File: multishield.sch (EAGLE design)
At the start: 18 parts, among them CN1 3P-2.54-90D, J2 2x16p-2.54, J4 2x6p-2.54, K2 TS-1101F, M1 ARDUINO_R3_ICSP, SW1 SK-12D01, U1 AD595AQ-DIP14, U2 ATMEGA328P_PDIP, Y1 16MHZ

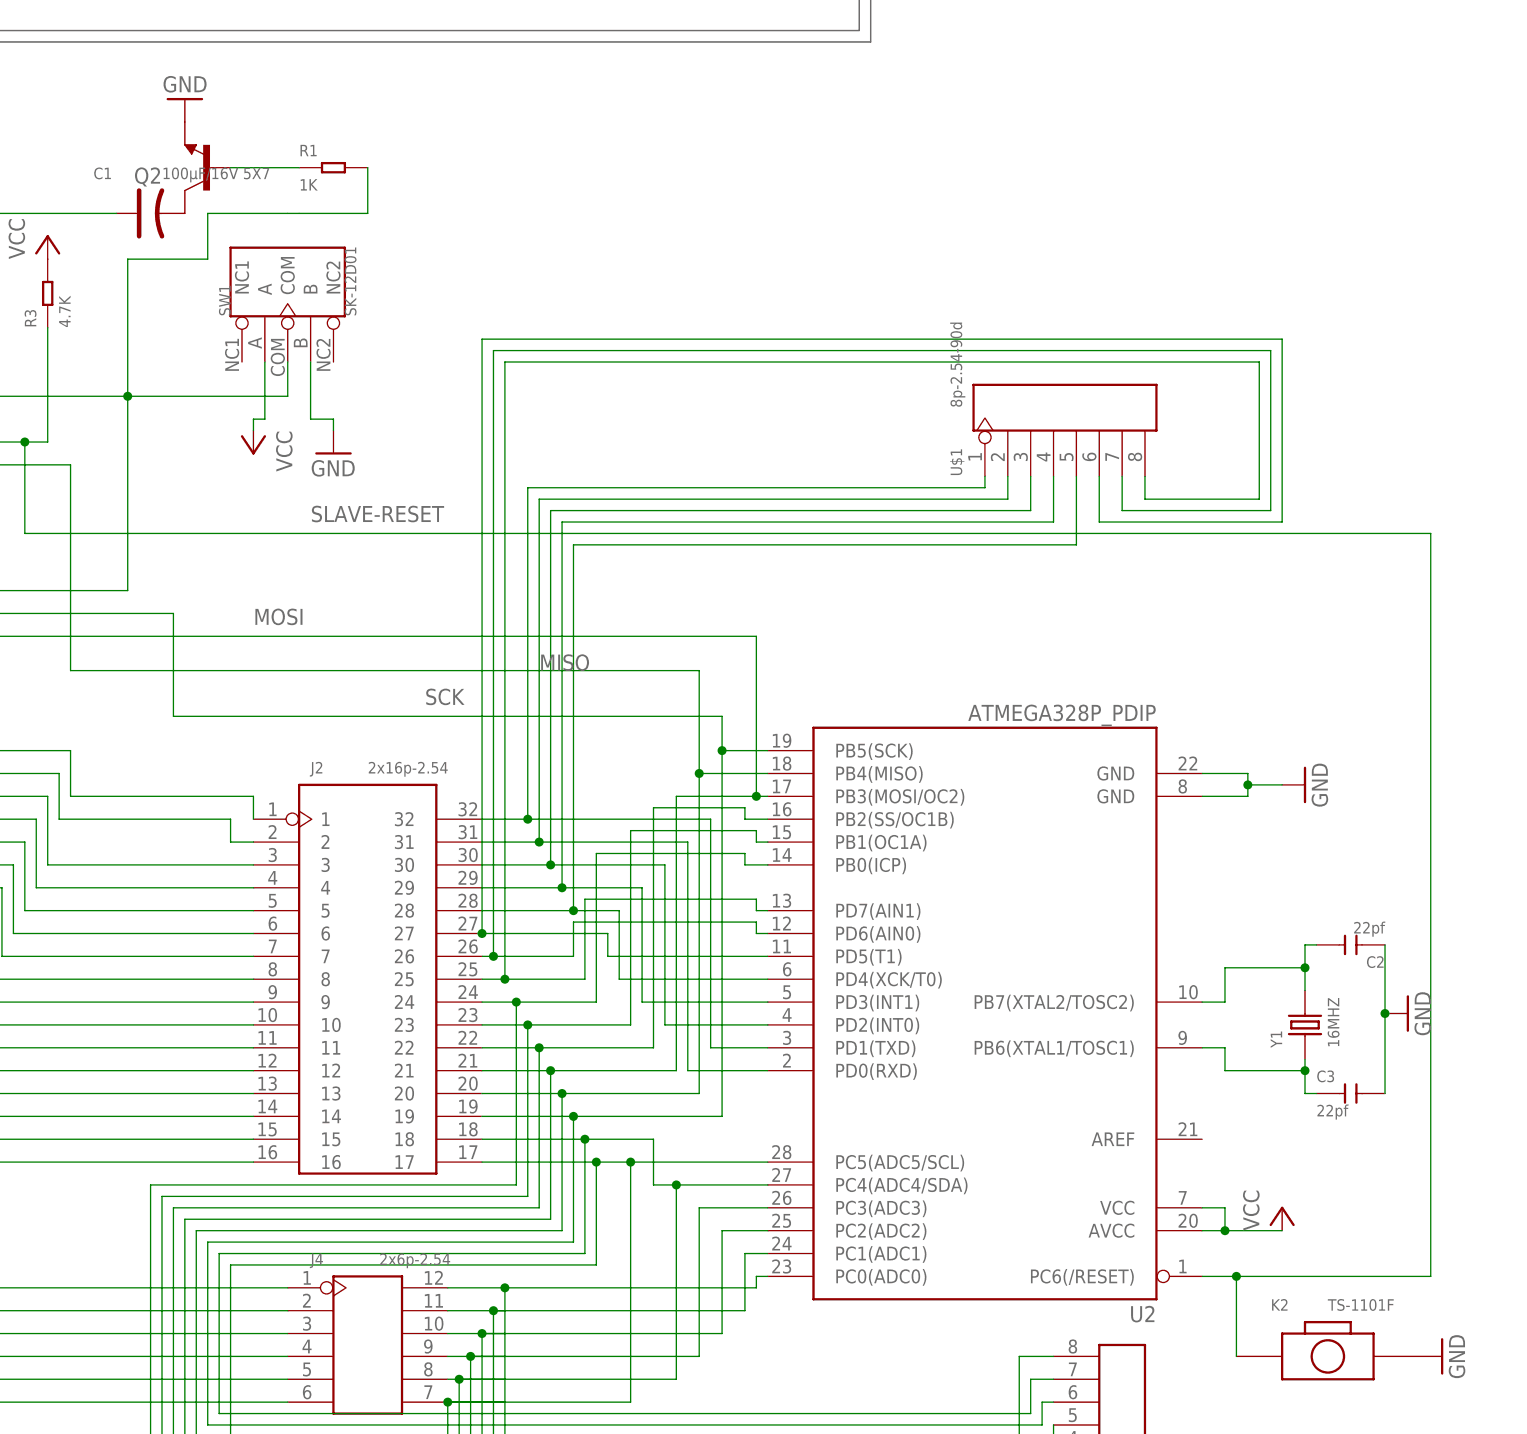
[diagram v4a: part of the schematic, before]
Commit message: adding 100nF capacitors and minor other changes
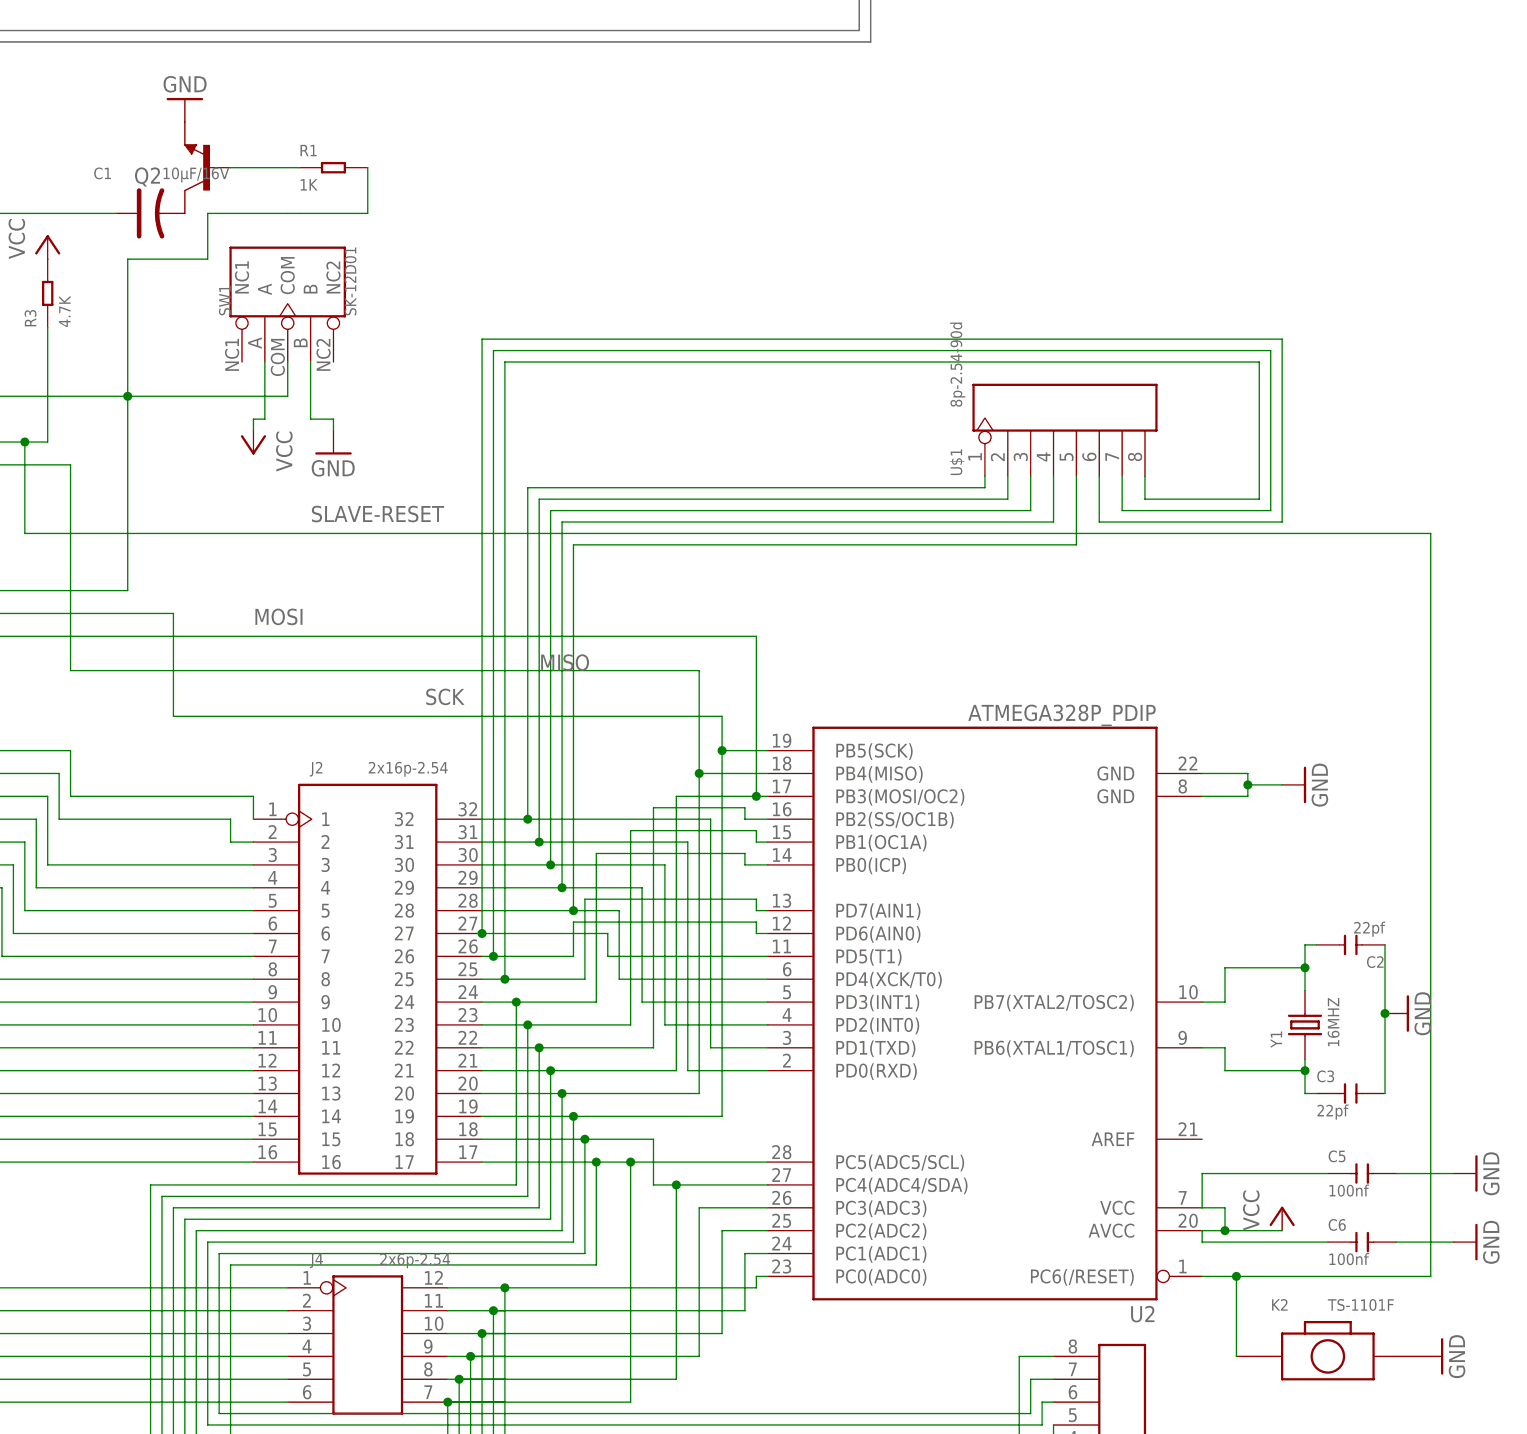
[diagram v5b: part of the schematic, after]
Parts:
- added C5, C6: 100nf, Seeed-OPL-Capacitor:DIP-CERAMIC-DISC-100NF-50V-Y5V(D5.0MM)
- C1: value 100µF/16V 5X7 -> 10µF/16V
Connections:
- net GND: now also C5.2, C6.2
- net VCC: now also C5.1, C6.1
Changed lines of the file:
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@@
 <setting verticaltext="up"/>
 </settings>
-<grid distance="0.05" unitdist="inch" unit="inch" style="lines" multiple="1" display="no" altdistance="0.01" altunitdist="inch" altunit="inch"/>
+<grid distance="0.1" unitdist="inch" unit="inch" style="lines" multiple="1" display="no" altdistance="0.01" altunitdist="inch" altunit="inch"/>
 <layers>
 <layer number="1" name="Top" color="4" fill="1" visible="no" active="no"/>
@@
 <part name="GND11" library="supply1" deviceset="GND" device=""/>
 <part name="K2" library="Seeed-OPL-Button" deviceset="DIP-BUTTON-FRONT-WHITE(2P-3.4X6MM)" device="" value="TS-1101F"/>
-<part name="C1" library="Seeed-OPL-Capacitor" deviceset="DIP-CAP-ALUMINUM-47UF-16V(D5-H9MM)" device="" value="100µF/16V  5X7"/>
+<part name="C1" library="Seeed-OPL-Capacitor" deviceset="DIP-CAP-ALUMINUM-47UF-16V(D5-H9MM)" device="" value="10µF/16V"/>
 <part name="GND5" library="supply1" deviceset="GND" device=""/>
 <part name="R1" library="Seeed-OPL-Resistor" deviceset="DIP-RES-1K-5%-1/4W(PR-D2.3XL6.5MM)" device="" value="1K"/>
@@
 <part name="Q2" library="SparkFun-DiscreteSemi" deviceset="TRANSISTOR_NPN" device="BC547"/>
 <part name="CN1" library="Seeed-OPL-Connector" deviceset="DIP-BLACK-FEMALE-HEADER(3P-2.54-90D)" device="" value="3P-2.54-90D"/>
+<part name="C5" library="Seeed-OPL-Capacitor" deviceset="DIP-CERAMIC-DISC-100NF-50V-Y5V(D5.0MM)" device="" value="100nf"/>
+<part name="C6" library="Seeed-OPL-Capacitor" deviceset="DIP-CERAMIC-DISC-100NF-50V-Y5V(D5.0MM)" device="" value="100nf"/>
+<part name="GND12" library="supply1" deviceset="GND" device=""/>
+<part name="GND13" library="supply1" deviceset="GND" device=""/>
 </parts>
 <sheets>
@@
 <instance part="Q2" gate="G$1" x="194.31" y="177.8" rot="R180"/>
 <instance part="CN1" gate="G$1" x="97.79" y="69.85"/>
+<instance part="C5" gate="G$1" x="322.58" y="66.04"/>
+<instance part="C6" gate="G$1" x="322.58" y="58.42"/>
+<instance part="GND12" gate="1" x="335.28" y="66.04" rot="R90"/>
+<instance part="GND13" gate="1" x="335.28" y="58.42" rot="R90"/>
 </instances>
 <busses>
@@
 <pinref part="U2" gate="G$1" pin="AVCC"/>
 <pinref part="P+2" gate="VCC" pin="VCC"/>
+<junction x="307.34" y="59.69"/>
 <wire x1="304.8" y1="59.69" x2="307.34" y2="59.69" width="0.1524" layer="91"/>
-<junction x="307.34" y="59.69"/>
 <wire x1="307.34" y1="59.69" x2="313.69" y2="59.69" width="0.1524" layer="91"/>
 <pinref part="U2" gate="G$1" pin="VCC"/>
 <wire x1="304.8" y1="62.23" x2="307.34" y2="62.23" width="0.1524" layer="91"/>
 <wire x1="307.34" y1="62.23" x2="307.34" y2="59.69" width="0.1524" layer="91"/>
+<pinref part="C5" gate="G$1" pin="1"/>
+<wire x1="318.77" y1="66.04" x2="304.8" y2="66.04" width="0.1524" layer="91"/>
+<wire x1="304.8" y1="66.04" x2="304.8" y2="62.23" width="0.1524" layer="91"/>
+<pinref part="C6" gate="G$1" pin="1"/>
+<wire x1="318.77" y1="58.42" x2="304.8" y2="58.42" width="0.1524" layer="91"/>
+<wire x1="304.8" y1="58.42" x2="304.8" y2="59.69" width="0.1524" layer="91"/>
 </segment>
 <segment>
@@
 <pinref part="CN1" gate="G$1" pin="P$3"/>
 </segment>
-</net>
+<segment>
+<pinref part="C5" gate="G$1" pin="2"/>
+<pinref part="GND12" gate="1" pin="GND"/>
+<wire x1="332.74" y1="66.04" x2="326.39" y2="66.04" width="0.1524" layer="91"/>
+</segment>
+<segment>
+<pinref part="C6" gate="G$1" pin="2"/>
+<pinref part="GND13" gate="1" pin="GND"/>
+<wire x1="332.74" y1="58.42" x2="326.39" y2="58.42" width="0.1524" layer="91"/>
+</segment>
+</net>

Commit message: rev 1
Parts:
- C1: value 10µF/16V -> 10µF
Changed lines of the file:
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@@
 <part name="GND11" library="supply1" deviceset="GND" device=""/>
 <part name="K2" library="Seeed-OPL-Button" deviceset="DIP-BUTTON-FRONT-WHITE(2P-3.4X6MM)" device="" value="TS-1101F"/>
-<part name="C1" library="Seeed-OPL-Capacitor" deviceset="DIP-CAP-ALUMINUM-47UF-16V(D5-H9MM)" device="" value="10µF/16V"/>
+<part name="C1" library="Seeed-OPL-Capacitor" deviceset="DIP-CAP-ALUMINUM-47UF-16V(D5-H9MM)" device="" value="10µF"/>
 <part name="GND5" library="supply1" deviceset="GND" device=""/>
 <part name="R1" library="Seeed-OPL-Resistor" deviceset="DIP-RES-1K-5%-1/4W(PR-D2.3XL6.5MM)" device="" value="1K"/>

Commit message: latest updates
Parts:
- added J1, J3, J5, J6: 7p-2.54-90d, Seeed-OPL-Connector:DIP-BLACK-MALE-HEADER(7P-2.54-90D)
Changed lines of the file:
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@@
 <setting verticaltext="up"/>
 </settings>
-<grid distance="0.1" unitdist="inch" unit="inch" style="lines" multiple="1" display="no" altdistance="0.01" altunitdist="inch" altunit="inch"/>
+<grid distance="0.05" unitdist="inch" unit="inch" style="lines" multiple="1" display="no" altdistance="0.01" altunitdist="inch" altunit="inch"/>
 <layers>
 <layer number="1" name="Top" color="4" fill="1" visible="no" active="no"/>
@@
 <part name="GND12" library="supply1" deviceset="GND" device=""/>
 <part name="GND13" library="supply1" deviceset="GND" device=""/>
+<part name="J1" library="Seeed-OPL-Connector" deviceset="DIP-BLACK-MALE-HEADER(7P-2.54-90D)" device="" value="7p-2.54-90d"/>
+<part name="J3" library="Seeed-OPL-Connector" deviceset="DIP-BLACK-MALE-HEADER(7P-2.54-90D)" device="" value="7p-2.54-90d"/>
+<part name="J5" library="Seeed-OPL-Connector" deviceset="DIP-BLACK-MALE-HEADER(7P-2.54-90D)" device="" value="7p-2.54-90d"/>
+<part name="J6" library="Seeed-OPL-Connector" deviceset="DIP-BLACK-MALE-HEADER(7P-2.54-90D)" device="" value="7p-2.54-90d"/>
 </parts>
 <sheets>
@@
 <instance part="GND12" gate="1" x="335.28" y="66.04" rot="R90"/>
 <instance part="GND13" gate="1" x="335.28" y="58.42" rot="R90"/>
+<instance part="J1" gate="G$1" x="287.02" y="170.18" rot="R90"/>
+<instance part="J3" gate="G$1" x="260.35" y="5.08"/>
+<instance part="J5" gate="G$1" x="313.69" y="27.94"/>
+<instance part="J6" gate="G$1" x="316.23" y="170.18" rot="R90"/>
 </instances>
 <busses>

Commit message: 7pin angled headers instead
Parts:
- removed CN1: 3P-2.54-90D, Seeed-OPL-Connector:DIP-BLACK-FEMALE-HEADER(3P-2.54-90D)
- removed U$1, U$2, U$3: 8p-2.54-90d, Seeed-OPL-Connector:DIP-BLACK-FEMALE-HEADER-R/A(8P-2.54-90D)
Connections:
- net GND: now also J6.5, J6.6, K2.1; no longer CN1.P$3, K2.2, U$3.8
- net MISO: now also J5.4; no longer U$2.5
- net MOSI: now also J5.3; no longer U$2.4
- net N$25: now also J1.1; no longer U$1.1
- net N$26: now also J1.2; no longer U$1.2
- net N$27: now also J1.3; no longer U$1.3
- net N$28: now also J1.4; no longer U$1.4
- net N$29: now also J1.5; no longer U$1.5
- net N$30: now also J1.6; no longer U$1.6
- net N$32: now also J3.1; no longer U$1.8
- net N$33: now also J6.7; no longer U$2.1
- net N$34: now also J5.1; no longer U$2.2
- net N$35: now also J5.2; no longer U$2.3
- net N$41: now also J1.7; no longer U$1.7
- net N$45: now also J3.2; no longer U$3.1
- net N$46: now also J3.3; no longer U$3.2
- net N$47: now also J3.4; no longer U$3.3
- net N$48: now also J3.5; no longer U$3.4
- net N$49: now also J3.6, J5.6; no longer U$2.7, U$3.5
- net N$50: now also J3.7, J5.7; no longer U$2.8, U$3.6
- net N$54: now also J6.3, J6.4; no longer CN1.P$1
- net SCK: now also J5.5; no longer U$2.6
- net SLAVE-RESET: now also K2.2; no longer K2.1
- net VCC: now also J6.1, J6.2; no longer CN1.P$2, U$3.7
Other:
- moved on the sheet: J1, J3, J5, J6, K2
